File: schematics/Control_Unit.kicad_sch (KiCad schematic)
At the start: 50 parts, among them SW1 SW_Push, U1 28C256, U2 28C256, U3 74LS161, U5 74LS00, U6 74LS04, U7 74LS04

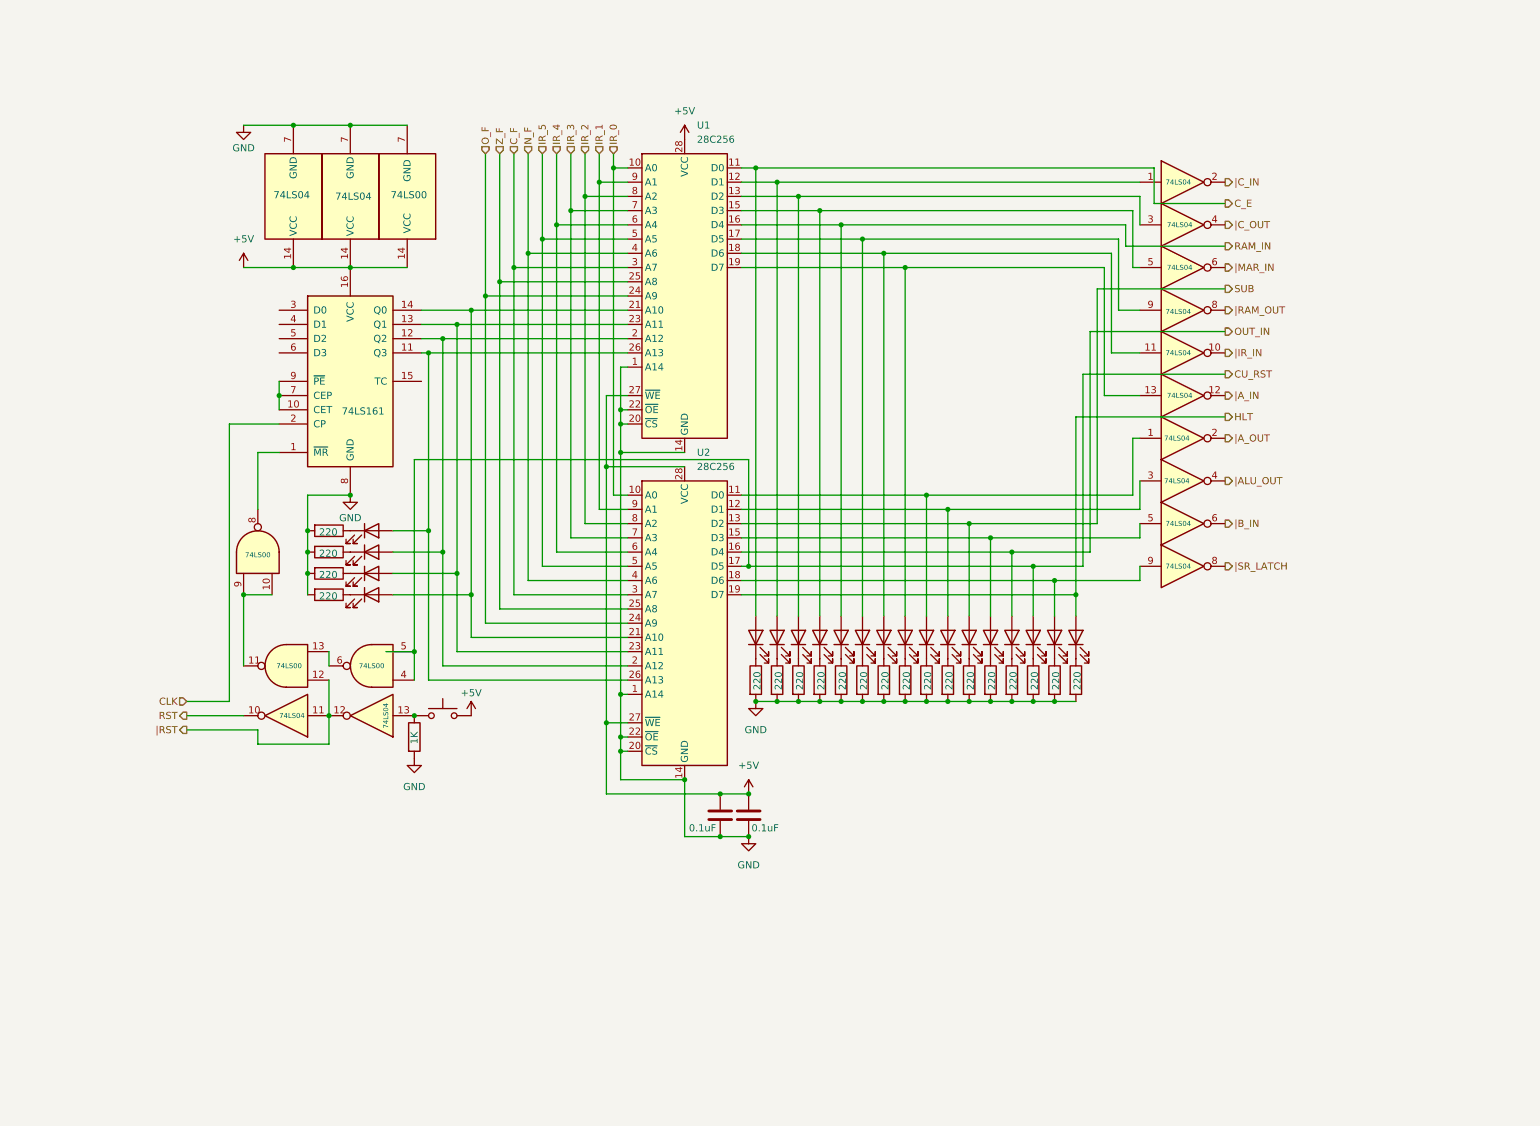
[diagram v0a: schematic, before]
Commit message: feat: updated electrical diagrams & individual part list
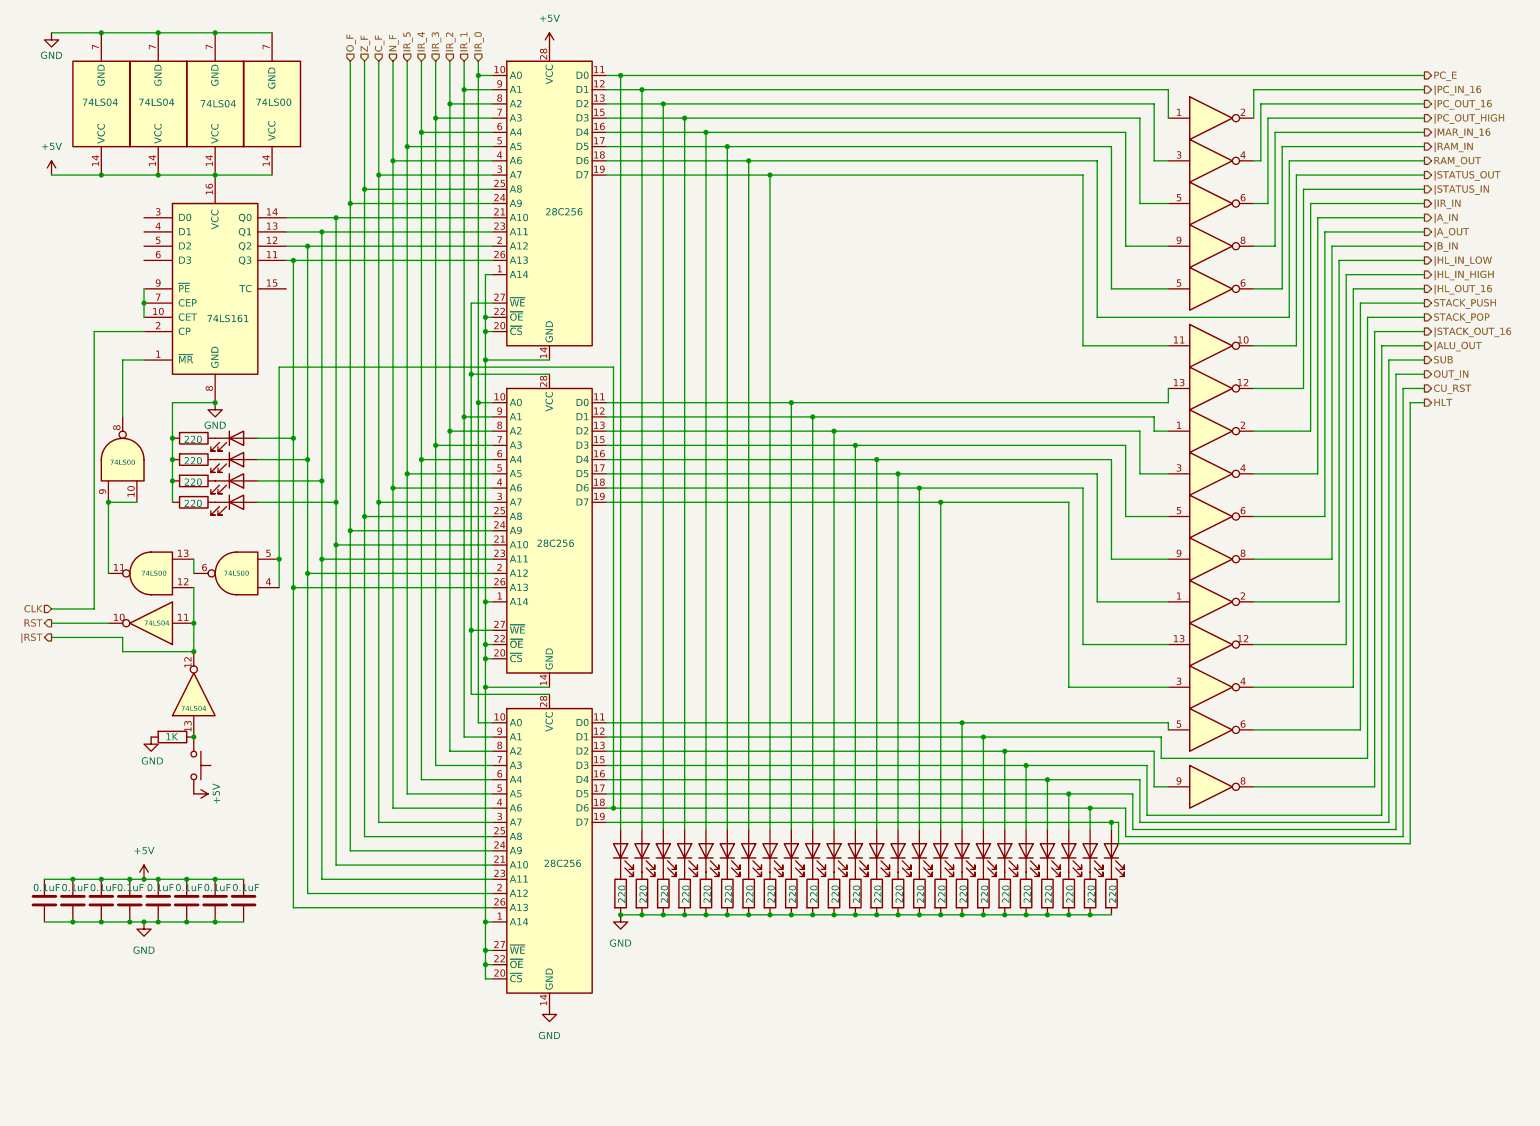
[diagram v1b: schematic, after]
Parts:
- added C3, C4, C5, C6, C7, C8: 0.1uF, symbol Device:C
- added D18, D19, D20, D21, D22, D23, D24, D25: LED, symbol Device:LED
- added R19, R20, R21, R22, R23, R24, R25, R26: 220, symbol Device:R
- added U4: 28C256, symbol Memory_EEPROM:28C256
- added U8, U9: 74LS04, symbol 74xx:74LS04
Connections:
- net |SR_LATCH is gone; now on net |B_IN: U7.8
- net +5V: now also C3.1, C4.1, C5.1, C6.1, C7.1, C8.1, U8.14 (VCC); no longer U1.27 (~{WE}), U2.27 (~{WE}), U2.28 (VCC)
- net CU_RST: now also D24.2 (A), U4.18 (D6); no longer D14.2 (A), U2.17 (D5)
- net C_F: now also U4.3 (A7)
- net GND: now also C3.2, C4.2, C5.2, C6.2, C7.2, C8.2, R19.2, R20.2, R21.2, R22.2, R23.2, R24.2, R25.2, R26.2, U4.14 (GND), U8.7 (GND); no longer U1.1 (A14), U1.14 (GND), U1.20 (~{CS}), U1.22 (~{OE}), U2.1 (A14), U2.14 (GND), U2.20 (~{CS}), U2.22 (~{OE})
- net HLT: now also D25.2 (A), U4.19 (D7); no longer D16.2 (A), U2.19 (D7)
- net IR_0: now also U4.10 (A0)
- net IR_1: now also U4.9 (A1)
- net IR_2: now also U4.8 (A2)
- net IR_3: now also U4.7 (A3)
- net IR_4: now also U4.6 (A4)
- net IR_5: now also U4.5 (A5)
- net N_F: now also U4.4 (A6)
- net OUT_IN: now also D23.2 (A), U4.17 (D5); no longer D13.2 (A), U2.16 (D4)
- net O_F: now also U4.24 (A9)
- net SUB: now also D22.2 (A), U4.16 (D4); no longer D11.2 (A), U2.13 (D2)
- net Z_F: now also U4.25 (A8)
- net |ALU_OUT: now also D21.2 (A), U4.15 (D3); no longer U7.4
- net |A_IN: now also U7.4; no longer U6.12
- net |A_OUT: now also U7.6; no longer U7.2
- net |B_IN: no longer U7.6
- net |IR_IN: now also U7.2; no longer U6.10
- net at D29.2 (A), U1.26 (A13), U2.26 (A13)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: now also U4.26 (A13)
- net at D30.2 (A), U1.2 (A12), U2.2 (A12)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: now also U4.2 (A12)
- net at D28.2 (A), U1.23 (A11), U2.23 (A11)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: now also U4.23 (A11)
- net at D17.2 (A), U1.21 (A10), U2.21 (A10)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: now also U4.21 (A10)
- net at D8.2 (A), U1.19 (D7): now also U6.11; no longer U6.13
- net at D10.2 (A), U2.12 (D1): now also U7.1; no longer U7.3
- net at D9.2 (A), U2.11 (D0): now also U6.13; no longer U7.1
- net at D15.2 (A), U2.18 (D6): now also U8.13; no longer U7.9
- net at D6.2 (A), U1.17 (D5): now also U9.5; no longer U6.9
- net RAM_OUT: now reaches D7.2 (A), U1.18 (D6)
- net RAM_OUT: no longer U6.11
- net C_E renamed PC_E
- net RAM_IN: no longer names the net of D5.2 (A), U1.16 (D4)
- net RAM_IN: now also U6.9
- net |C_IN renamed |PC_IN_16
- net |C_OUT renamed |PC_OUT_16
- net |MAR_IN renamed |PC_OUT_HIGH
- net |RAM_OUT renamed |MAR_IN_16
- new net: D18.1 (K), R19.1
- new net: D23.1 (K), R24.1
- new net: D14.2 (A), U2.17 (D5), U8.1
- new net: D16.2 (A), U2.19 (D7), U8.3
- new net: D19.1 (K), R20.1
- new net: D24.1 (K), R25.1
- new net: D25.1 (K), R26.1
- new net: U1.1 (A14), U1.14 (GND), U1.20 (~{CS}), U1.22 (~{OE}), U2.1 (A14), U2.14 (GND), U2.20 (~{CS}), U2.22 (~{OE}), U4.1 (A14), U4.20 (~{CS}), U4.22 (~{OE}), U4.27 (~{WE})
- new net: D11.2 (A), U2.13 (D2), U7.3
- new net: D13.2 (A), U2.16 (D4), U7.9
- new net: U1.27 (~{WE}), U2.27 (~{WE}), U2.28 (VCC), U4.28 (VCC)
- new net: D18.2 (A), U4.11 (D0), U8.5
- new net: D20.2 (A), U4.13 (D2), U8.9
- new net: D20.1 (K), R21.1
- new net: D22.1 (K), R23.1
- new net: D21.1 (K), R22.1
- new net STACK_POP: D19.2 (A), U4.12 (D1)
- new net STACK_PUSH: U8.6
- new net |HL_IN_HIGH: U8.12
- new net |HL_IN_LOW: U8.2
- new net |HL_OUT_16: U8.4
- new net |RAM_IN: U9.6
- new net |STACK_OUT_16: U8.8
- new net |STATUS_IN: U6.12
- new net |STATUS_OUT: U6.10

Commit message: chore: full part list & memory module rework
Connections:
- net RAM_IN: now reaches D6.2 (A), U1.17 (D5)
- net RAM_IN: no longer U9.5
- net RAM_OUT: no longer names the net of D7.2 (A), U1.18 (D6)
- net RAM_OUT: now also U9.5
- net |RAM_IN renamed |RAM_OUT
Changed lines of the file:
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@@
 	(wire
 		(pts
-			(xy 205.74 66.04) (xy 240.03 66.04)
-		)
-		(stroke
-			(width 0)
-			(type default)
-		)
-	)
-	(wire
-		(pts
 			(xy 60.96 55.88) (xy 62.23 55.88)
 		)
@@
 	(wire
 		(pts
+			(xy 233.68 63.5) (xy 240.03 63.5)
+		)
+		(stroke
+			(width 0)
+			(type default)
+		)
+	)
+	(wire
+		(pts
 			(xy 27.94 173.99) (xy 33.02 173.99)
 		)
@@
 	(wire
 		(pts
+			(xy 240.03 63.5) (xy 240.03 38.1)
+		)
+		(stroke
+			(width 0)
+			(type default)
+		)
+	)
+	(wire
+		(pts
 			(xy 209.55 160.02) (xy 209.55 156.21)
 		)
@@
 	(wire
 		(pts
-			(xy 238.76 35.56) (xy 238.76 60.96)
+			(xy 238.76 35.56) (xy 238.76 58.42)
 		)
 		(stroke
@@
 	(wire
 		(pts
-			(xy 205.74 66.04) (xy 205.74 38.1)
-		)
-		(stroke
-			(width 0)
-			(type default)
-		)
-	)
-	(wire
-		(pts
 			(xy 19.05 15.24) (xy 27.94 15.24)
 		)
@@
 	(wire
 		(pts
-			(xy 240.03 66.04) (xy 240.03 38.1)
-		)
-		(stroke
-			(width 0)
-			(type default)
-		)
-	)
-	(wire
-		(pts
 			(xy 200.66 132.08) (xy 218.44 132.08)
 		)
@@
 	(wire
 		(pts
-			(xy 238.76 60.96) (xy 233.68 60.96)
-		)
-		(stroke
-			(width 0)
-			(type default)
-		)
-	)
-	(wire
-		(pts
 			(xy 162.56 88.9) (xy 162.56 157.48)
 		)
@@
 	(wire
 		(pts
+			(xy 205.74 63.5) (xy 218.44 63.5)
+		)
+		(stroke
+			(width 0)
+			(type default)
+		)
+	)
+	(wire
+		(pts
 			(xy 38.1 40.64) (xy 48.26 40.64)
 		)
@@
 	(wire
 		(pts
-			(xy 208.28 60.96) (xy 208.28 35.56)
+			(xy 208.28 58.42) (xy 208.28 35.56)
 		)
 		(stroke
@@
 	(wire
 		(pts
+			(xy 205.74 63.5) (xy 205.74 38.1)
+		)
+		(stroke
+			(width 0)
+			(type default)
+		)
+	)
+	(wire
+		(pts
 			(xy 118.11 40.64) (xy 147.32 40.64)
 		)
@@
 	(wire
 		(pts
-			(xy 208.28 60.96) (xy 218.44 60.96)
+			(xy 208.28 58.42) (xy 238.76 58.42)
 		)
 		(stroke
@@
 		)
 	)
-	(hierarchical_label "|RAM_IN"
+	(hierarchical_label "RAM_IN"
 		(shape output)
 		(at 264.16 35.56 0)
@@
 		)
 	)
-	(hierarchical_label "RAM_OUT"
+	(hierarchical_label "|RAM_OUT"
 		(shape output)
 		(at 264.16 38.1 0)
@@
 	)
 	(symbol
-		(lib_id "74xx:74LS04")
-		(at 226.06 60.96 0)
-		(unit 3)
-		(exclude_from_sim no)
-		(in_bom yes)
-		(on_board yes)
-		(dnp no)
-		(fields_autoplaced yes)
-		(property "Reference" "U9"
-			(at 226.06 52.07 0)
-			(effects
-				(font
-					(size 1.27 1.27)
-				)
-				(hide yes)
-			)
-		)
-		(property "Value" "74LS04"
-			(at 226.06 54.61 0)
-			(effects
-				(font
-					(size 1.27 1.27)
-				)
-				(hide yes)
-			)
-		)
-		(property "Footprint" ""
-			(at 226.06 60.96 0)
-			(effects
-				(font
-					(size 1.27 1.27)
-				)
-				(hide yes)
-			)
-		)
-		(property "Datasheet" "http://www.ti.com/lit/gpn/sn74LS04"
-			(at 226.06 60.96 0)
-			(effects
-				(font
-					(size 1.27 1.27)
-				)
-				(hide yes)
-			)
-		)
-		(property "Description" "Hex Inverter"
-			(at 226.06 60.96 0)
-			(effects
-				(font
-					(size 1.27 1.27)
-				)
-				(hide yes)
-			)
-		)
-		(pin "8"
-		)
-		(pin "14"
-		)
-		(pin "1"
-		)
-		(pin "10"
-		)
-		(pin "7"
-		)
-		(pin "3"
-		)
-		(pin "9"
-		)
-		(pin "11"
-		)
-		(pin "2"
-		)
-		(pin "13"
-		)
-		(pin "6"
-		)
-		(pin "4"
-		)
-		(pin "12"
-		)
-		(pin "5"
-		)
-		(instances
-			(project "Control_Unit"
-				(path "/00881835-431f-440c-8b02-f05a8dfd3447"
-					(reference "U9")
-					(unit 3)
-				)
-			)
-		)
-	)
-	(symbol
 		(lib_id "Device:R")
 		(at 170.18 168.91 0)
@@
 				)
 			)
+		)
+	)
+	(symbol
+		(lib_id "74xx:74LS04")
+		(at 226.06 63.5 0)
+		(unit 3)
+		(exclude_from_sim no)
+		(in_bom yes)
+		(on_board yes)
+		(dnp no)
+		(fields_autoplaced yes)
+		(property "Reference" "U9"
+			(at 226.06 54.61 0)
+			(effects
+				(font
+					(size 1.27 1.27)
+				)
+				(hide yes)
+			)
+		)
+		(property "Value" "74LS04"
+			(at 226.06 57.15 0)
+			(effects
+				(font
+					(size 1.27 1.27)
+				)
+				(hide yes)
+			)
+		)
+		(property "Footprint" ""
+			(at 226.06 63.5 0)
+			(effects
+				(font
+					(size 1.27 1.27)
+				)
+				(hide yes)
+			)
+		)
+		(property "Datasheet" "http://www.ti.com/lit/gpn/sn74LS04"
+			(at 226.06 63.5 0)
+			(effects
+				(font
+					(size 1.27 1.27)
+				)
+				(hide yes)
+			)
+		)
+		(property "Description" "Hex Inverter"
+			(at 226.06 63.5 0)
+			(effects
+				(font
+					(size 1.27 1.27)
+				)
+				(hide yes)
+			)
+		)
+		(pin "8"
+		)
+		(pin "14"
+		)
+		(pin "1"
+		)
+		(pin "10"
+		)
+		(pin "7"
+		)
+		(pin "3"
+		)
+		(pin "9"
+		)
+		(pin "11"
+		)
+		(pin "2"
+		)
+		(pin "13"
+		)
+		(pin "6"
+		)
+		(pin "4"
+		)
+		(pin "12"
+		)
+		(pin "5"
+		)
+		(instances
+			(project "Control_Unit"
+				(path "/00881835-431f-440c-8b02-f05a8dfd3447"
+					(reference "U9")
+					(unit 3)
+				)
+			)
